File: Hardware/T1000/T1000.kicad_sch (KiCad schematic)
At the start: 103 parts, among them J1 USB_C_Receptacle_USB2.0, J2 SOICbite, J3 XT30, J4 Nichrome, Q1 IRLML0060TRPBF, U1 LT3120JV-PBF, U2 RP2040, U3 W25Q128JVS, U4 LTC4419, U5 MAX-M10S, U6 MS5607-02BA, U7 LT6703CDC-3, U8 MAX77857, U9 XBee_SMT, Y1 445I23D12M00000

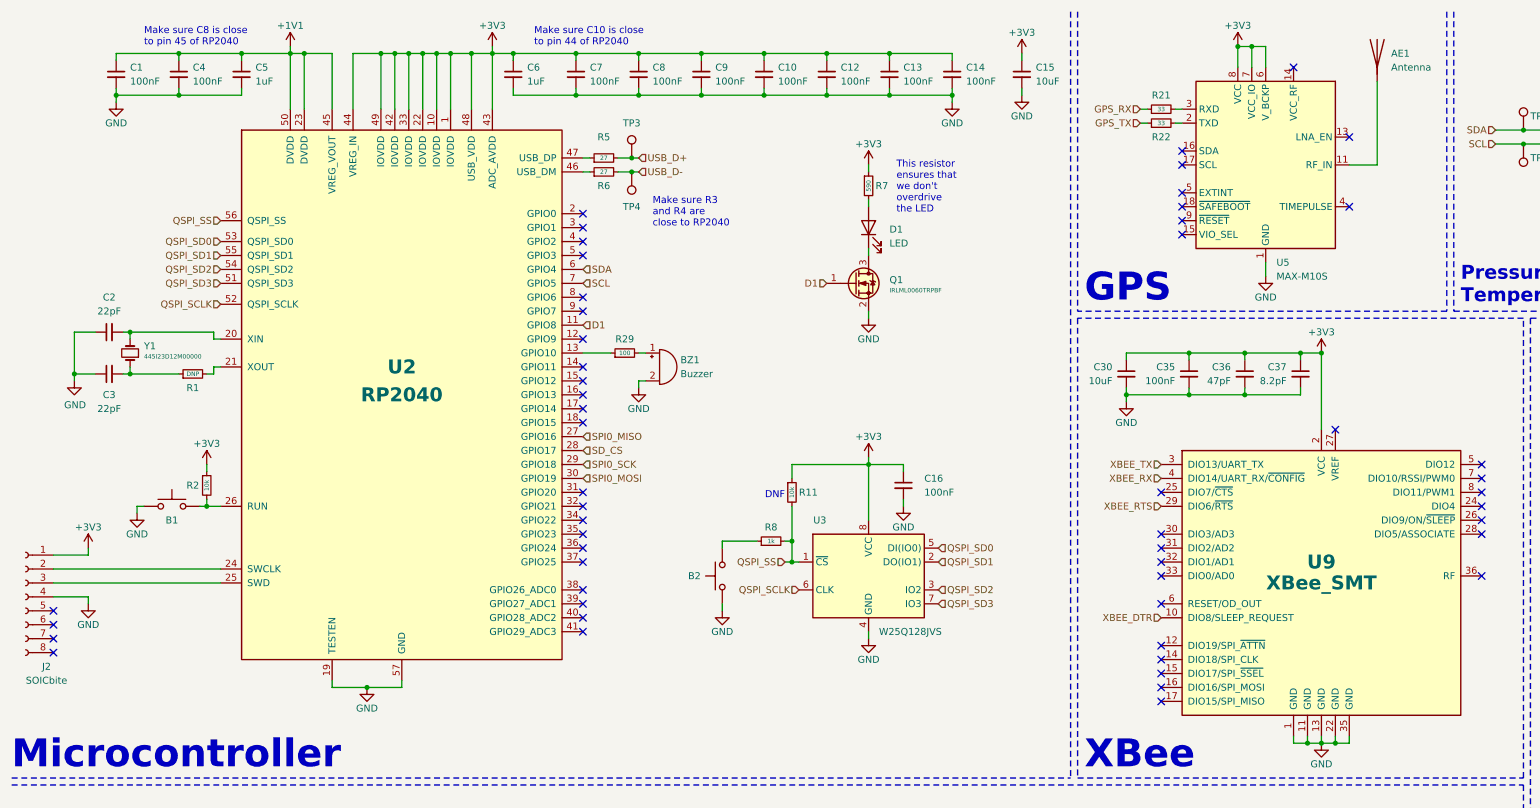
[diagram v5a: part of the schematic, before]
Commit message: little bit of routing, changed to MIA-M10 GPS to make my life harder
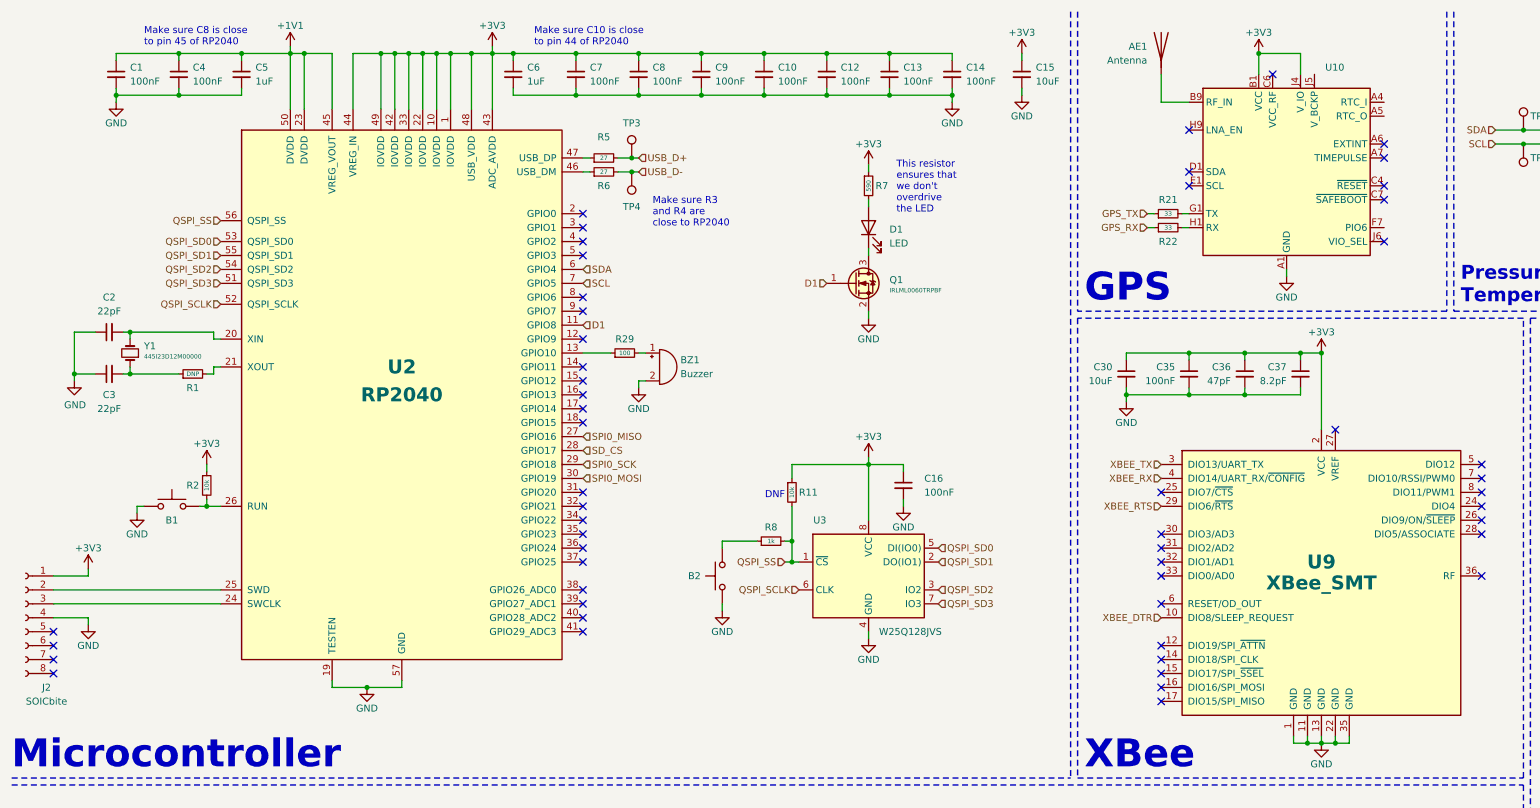
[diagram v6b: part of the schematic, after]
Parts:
- removed U5: MAX-M10S, RF_GPS:ublox_MAX, symbol RF_GPS:MAX-M10S
- added U10: ~, symbol Terminator_Lib:MIA-M10Q
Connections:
- net +3V3: now also U10.B1 (VCC), U10.J4 (V_IO)
- net GND: now also U10.A1 (GND), U10.A2 (GND), U10.A3 (GND), U10.A8 (GND), U10.A9 (GND), U10.B2 (GND), U10.B8 (GND), U10.C3 (GND), U10.C9 (GND), U10.E3 (GND), U10.E4 (GND), U10.E9 (GND), U10.F1 (GND), U10.F3 (GND), U10.F4 (GND), U10.G3 (GND), U10.G4 (GND), U10.G5 (GND), U10.G6 (GND), U10.H8 (GND), U10.J8 (GND), U10.J9 (GND)
- net GPS_RX: now also R22.1; no longer R21.1
- net GPS_TX: now also R21.1; no longer R22.1
- net at AE1.1 (A): now also U10.B9 (RF_IN)
- net at U2.24 (SWCLK): now also J2.3 (Pin_3); no longer J2.2 (Pin_2)
- net at U2.25 (SWD): now also J2.2 (Pin_2); no longer J2.3 (Pin_3)
- net at R22.2: now also U10.H1 (RX)
- net at R21.2: now also U10.G1 (TX)
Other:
- moved on the sheet: AE1, J2, R21, R22

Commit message: bringing it together, also managed to crash Kicad so this commit can be considered under duress in a court of law
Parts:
- added C43: 100nF, Capacitor_SMD:C_0603_1608Metric_Pad1.08x0.95mm_HandSolder, symbol Device:C_Small
- added R30, R31: 0, Resistor_SMD:R_0603_1608Metric_Pad0.98x0.95mm_HandSolder, symbol Device:R_Small
- added Y2: 32.768k, Crystal:Crystal_SMD_3215-2Pin_3.2x1.5mm, symbol Device:Crystal_Small
- R1: value DNP -> 1k
- U10: footprint (none) -> Terminator_Lib:MIA-M10Q
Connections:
- net +3V3: now also U10.J5 (V_BCKP), C43.1
- net GND: now also C43.2, R30.2, R31.2
- net GPS_RX: now also U2.15 (GPIO12)
- net GPS_TX: now also U2.16 (GPIO13)
- net at U10.A4 (RTC_I): now also Y2.2
- net at U10.A5 (RTC_O): now also Y2.1
- new net: R30.1, U10.F9 (RSRVD)
- new net: R31.1, U10.G7 (RSRVD)
- no-connect marks 62 -> 61
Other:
- moved on the sheet: AE1, BZ1, C21, C30, C32, C33, C34, C35, C36, C37, C38, C39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
